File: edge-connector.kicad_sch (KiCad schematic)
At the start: 25 parts, among them J9 dc-scm-rev-1-0-edge-connector

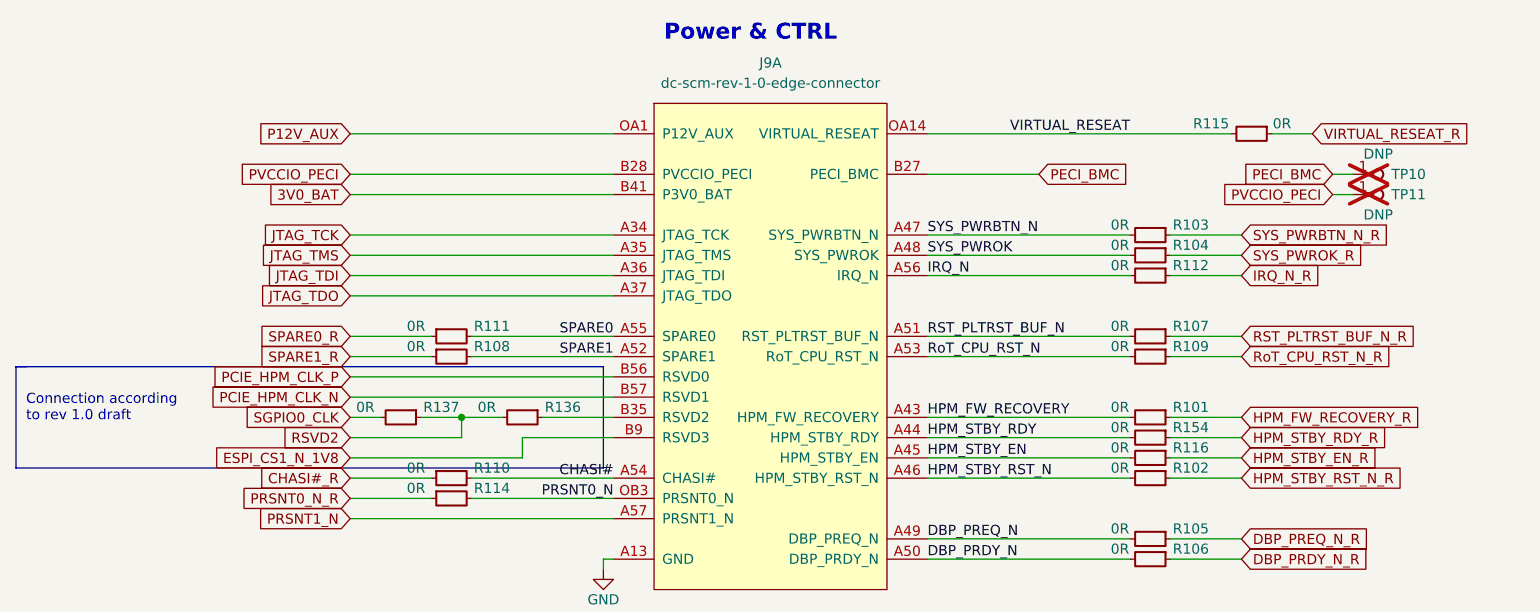
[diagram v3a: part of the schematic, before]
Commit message: [#68236] Remove DNP property from Testpoints
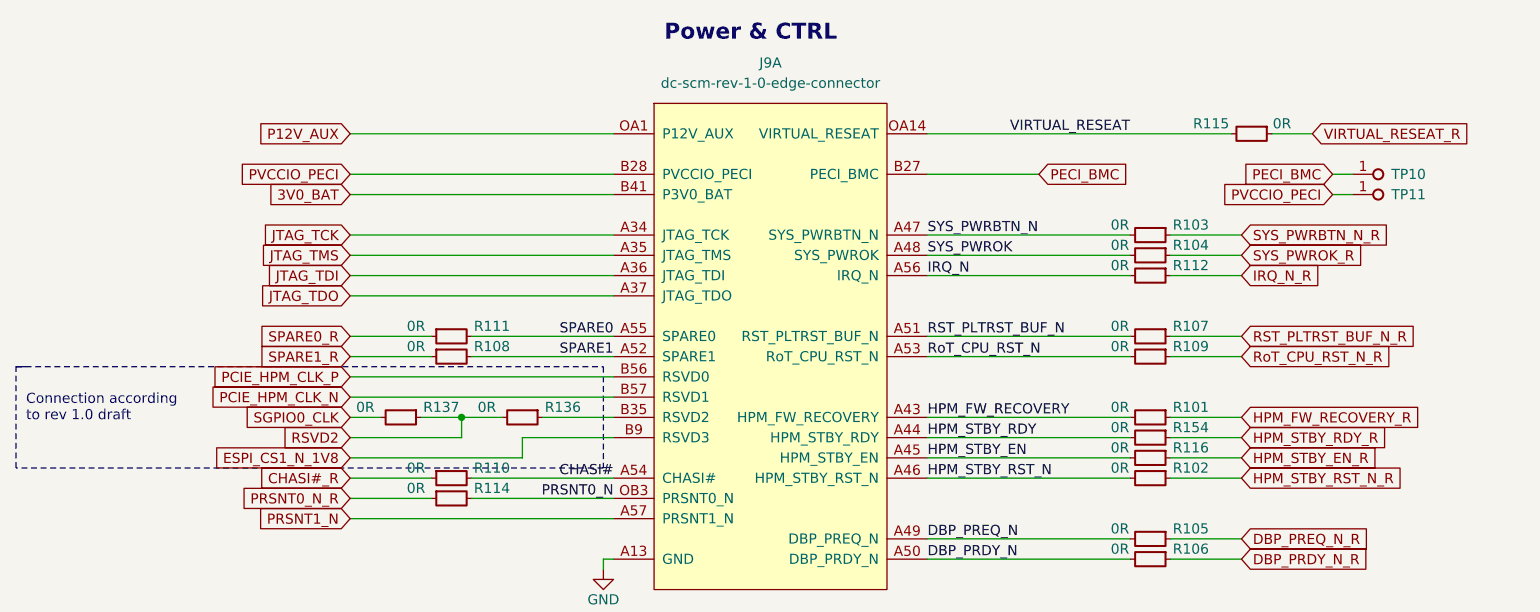
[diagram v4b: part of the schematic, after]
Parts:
- TP10, TP11: DNP DNP -> (none); now fitted
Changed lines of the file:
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@@
   )
   (polyline (pts (xy 33.02 77.47) (xy 106.68 77.47))
-    (stroke (width 0) (type default))
+    (stroke (width 0) (type dash))
   )
   (wire (pts (xy 274.32 54.61) (xy 274.32 66.04))
@@
   )
   (polyline (pts (xy 106.68 90.17) (xy 33.02 90.17))
-    (stroke (width 0) (type default))
+    (stroke (width 0) (type dash))
   )
   (wire (pts (xy 321.31 233.68) (xy 317.5 233.68))
@@
   )
   (polyline (pts (xy 106.68 77.47) (xy 106.68 90.17))
-    (stroke (width 0) (type default))
+    (stroke (width 0) (type dash))
   )
   (wire (pts (xy 317.5 186.69) (xy 321.31 186.69))
@@
   )
   (polyline (pts (xy 33.02 90.17) (xy 33.02 77.47))
-    (stroke (width 0) (type default))
+    (stroke (width 0) (type dash))
   )
   (wire (pts (xy 271.78 68.58) (xy 318.77 68.58))
@@
   )
   (symbol (lib_id "antmicroTestPoints:TP_1mm_SMD") (at 200.66 53.34 0) (mirror x) (unit 1)
-    (in_bom no) (on_board yes) (dnp yes)
+    (in_bom no) (on_board yes) (dnp no)
     (property "Reference" "TP10" (at 207.645 53.34 0)
       (effects (font (size 1.27 1.27)))
@@
     (property "License" "Apache-2.0" (at 215.9 35.56 0)
       (effects (font (size 1.27 1.27) (thickness 0.15)) (justify left bottom) hide)
-    )
-    (property "DNP" "DNP" (at 203.835 50.8 0)
-      (effects (font (size 1.27 1.27)))
     )
     (pin "1")
@@
   )
   (symbol (lib_id "antmicroTestPoints:TP_1mm_SMD") (at 200.66 55.88 0) (mirror x) (unit 1)
-    (in_bom no) (on_board yes) (dnp yes)
+    (in_bom no) (on_board yes) (dnp no)
     (property "Reference" "TP11" (at 207.645 55.88 0)
       (effects (font (size 1.27 1.27)))
@@
       (effects (font (size 1.27 1.27) (thickness 0.15)) (justify left bottom) hide)
     )
-    (property "DNP" "DNP" (at 203.835 58.42 0)
-      (effects (font (size 1.27 1.27)))
-    )
     (pin "1")
